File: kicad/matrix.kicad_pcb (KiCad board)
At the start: 2 copper layers, 20 parts, among them J1 Conn_01x08, Q1 2N7002DW-7-F, Q2 2N7002DW-7-F, Q3 2N7002DW-7-F, Q4 2N7002DW-7-F, Q5 2N7002DW-7-F, Q6 2N7002DW-7-F, Q7 2N7002DW-7-F, Q8 2N7002DW-7-F, U1 TLC59025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

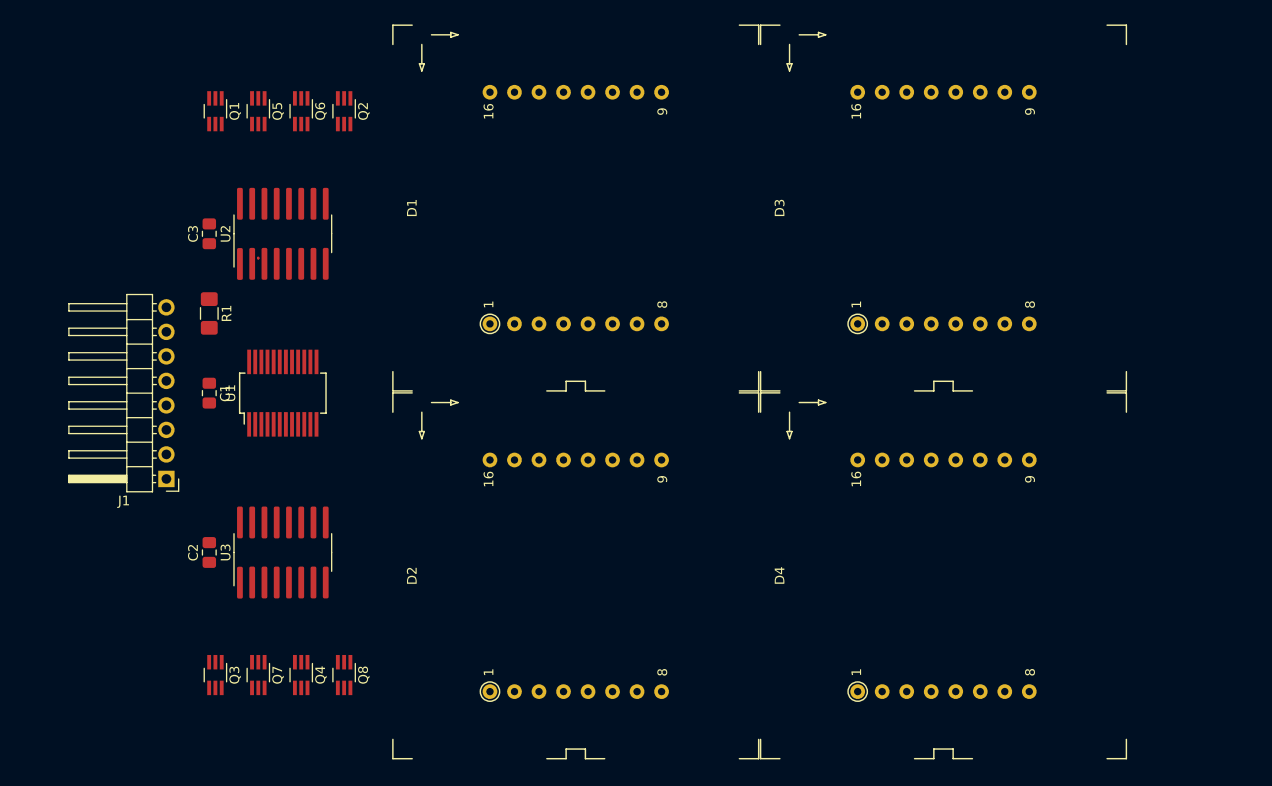
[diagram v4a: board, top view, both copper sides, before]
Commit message: OshPark design rules and copper GND pour
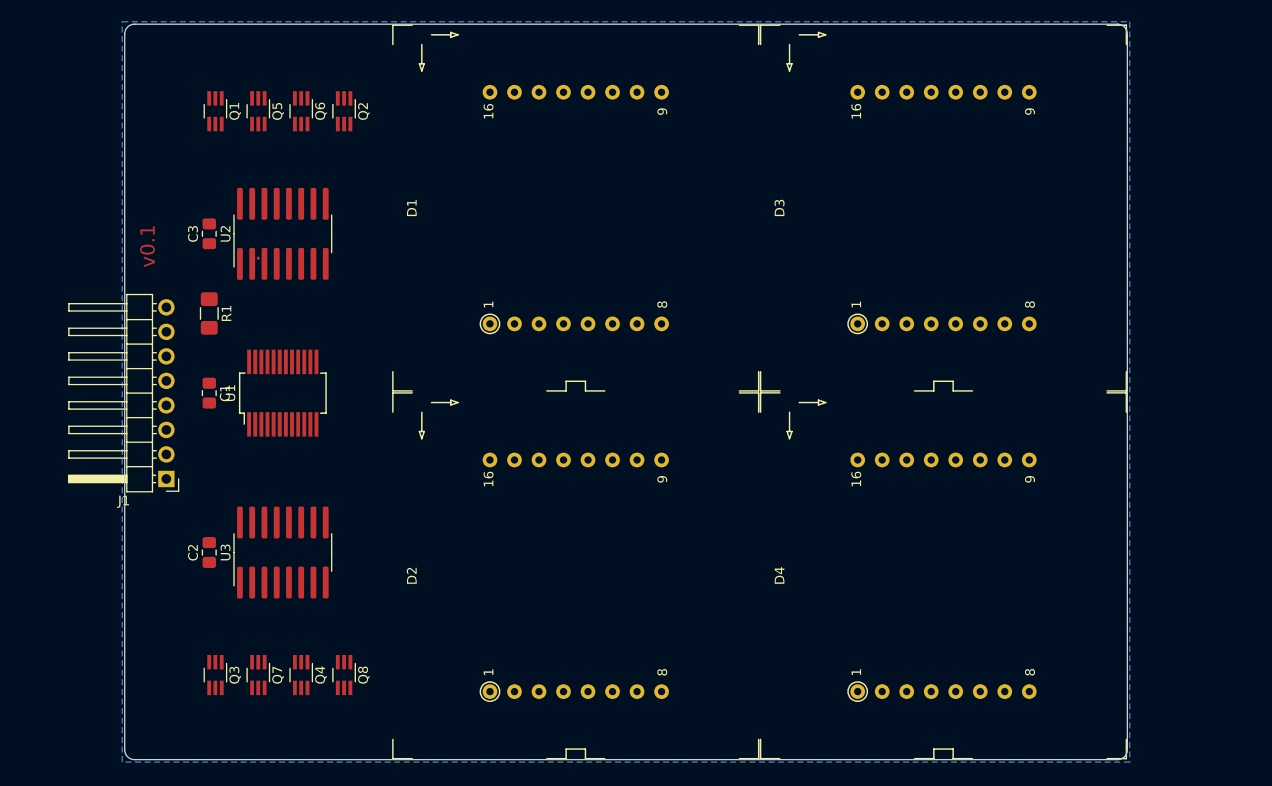
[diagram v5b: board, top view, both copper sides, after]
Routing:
- added copper zone on B.Cu, net GND
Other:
- board outline added: 103.9 x 76.2 mm
- net class Default: clearance 0.2 -> 0.1524; trace_width 0.25 -> 0.1524; via_dia 0.8 -> 0.508; via_drill 0.4 -> 0.254
- net class Power added: clearance 0.1524, trace_width 0.3048, via_dia 0.508, via_drill 0.254
- rule trace_clearance: 0.2 -> 0.1524
- rule trace_min: 0.2 -> 0.1524
- rule via_min_drill: 0.3 -> 0.254
- rule via_min_size: 0.4 -> 0.508
- board text added: "v0.1"
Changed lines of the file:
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@@
   (general
     (thickness 1.6)
-    (drawings 0)
+    (drawings 9)
     (tracks 2)
     (zones 0)
@@
     (0 F.Cu signal)
     (31 B.Cu signal)
-    (32 B.Adhes user)
-    (33 F.Adhes user)
-    (34 B.Paste user)
-    (35 F.Paste user)
     (36 B.SilkS user)
     (37 F.SilkS user)
     (38 B.Mask user)
     (39 F.Mask user)
-    (40 Dwgs.User user)
     (41 Cmts.User user)
-    (42 Eco1.User user)
-    (43 Eco2.User user)
     (44 Edge.Cuts user)
     (45 Margin user)
     (46 B.CrtYd user)
     (47 F.CrtYd user)
-    (48 B.Fab user)
-    (49 F.Fab user)
   )
   (setup
-    (last_trace_width 0.25)
-    (trace_clearance 0.2)
+    (last_trace_width 0.1524)
+    (user_trace_width 0.1524)
+    (user_trace_width 0.3048)
+    (trace_clearance 0.1524)
     (zone_clearance 0.508)
     (zone_45_only no)
-    (trace_min 0.2)
-    (via_size 0.8)
-    (via_drill 0.4)
-    (via_min_size 0.4)
-    (via_min_drill 0.3)
+    (trace_min 0.1524)
+    (via_size 0.508)
+    (via_drill 0.254)
+    (via_min_size 0.508)
+    (via_min_drill 0.254)
     (uvia_size 0.3)
     (uvia_drill 0.1)
@@
   (net 60 /ROWCLK)
   (net_class Default "This is the default net class."
-    (clearance 0.2)
-    (trace_width 0.25)
-    (via_dia 0.8)
-    (via_drill 0.4)
+    (clearance 0.1524)
+    (trace_width 0.1524)
+    (via_dia 0.508)
+    (via_drill 0.254)
     (uvia_dia 0.3)
     (uvia_drill 0.1)
@@
     (add_net "Net-(U3-Pad9)")
     (add_net VDD)
+  )
+  (net_class Power ""
+    (clearance 0.1524)
+    (trace_width 0.3048)
+    (via_dia 0.508)
+    (via_drill 0.254)
+    (uvia_dia 0.3)
+    (uvia_drill 0.1)
   )
   (module local:LED_8x8_3MM_38x38MM (layer F.Cu)
@@
     )
   )
+  (gr_text v0.1 (at 127.635 60.325 90) (layer F.Cu)
+    (effects (font (size 1.5 1.5) (thickness 0.3)))
+  )
+  (gr_arc (start 228.092 38.354) (end 229.108 38.354) (angle -90) (layer Edge.Cuts) (width 0.05))
+  (gr_arc (start 228.092 112.522) (end 228.092 113.538) (angle -90) (layer Edge.Cuts) (width 0.05))
+  (gr_arc (start 126.238 112.522) (end 125.222 112.522) (angle -90) (layer Edge.Cuts) (width 0.05))
+  (gr_arc (start 126.238 38.354) (end 126.238 37.338) (angle -90) (layer Edge.Cuts) (width 0.05))
+  (gr_line (start 126.238 37.338) (end 228.092 37.338) (layer Edge.Cuts) (width 0.05))
+  (gr_line (start 125.222 112.522) (end 125.222 38.354) (layer Edge.Cuts) (width 0.05))
+  (gr_line (start 228.092 113.538) (end 126.238 113.538) (layer Edge.Cuts) (width 0.05))
+  (gr_line (start 229.108 38.354) (end 229.108 112.522) (layer Edge.Cuts) (width 0.05))
   (segment (start 139.065 61.595) (end 139.05501 61.595) (width 0.25) (layer F.Cu) (net 0))
   (segment (start 139.05501 61.595) (end 139.05501 61.53) (width 0.25) (layer F.Cu) (net 0))
+  (zone (net 36) (net_name GND) (layer B.Cu) (hatch edge 0.508)
+    (connect_pads (clearance 0.508))
+    (min_thickness 0.254)
+    (fill yes (arc_segments 32) (thermal_gap 0.508) (thermal_bridge_width 0.508))
+    (polygon
+      (pts
+        (xy 229.362 113.792) (xy 124.968 113.792) (xy 124.968 37.084) (xy 229.362 37.084)
+      )
+    )
+  )
 )

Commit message: Wire up cathodes
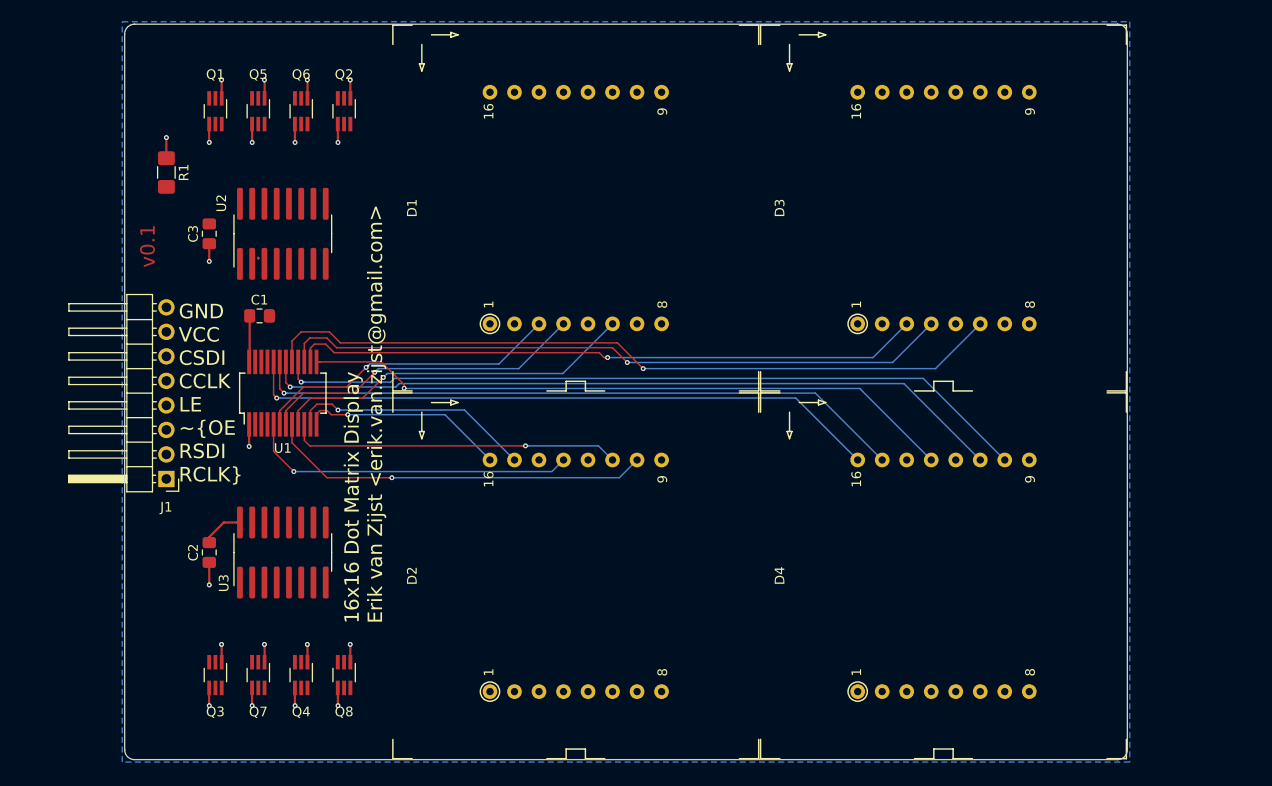
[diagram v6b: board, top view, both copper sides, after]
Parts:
- moved R1 15.3 mm to (129.5, 52.7)
- moved C1 9.55 mm to (139.2, 67.6), turned to 0 degrees
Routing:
- net /COL11: track 0.00 -> 78.8 mm, vias 0 -> 1
- net /COL13: track 0.00 -> 77.7 mm, vias 0 -> 1
- net /COL12: track 0.00 -> 77.4 mm, vias 0 -> 1
- net /COL10: track 0.00 -> 69.8 mm, vias 0 -> 1
- net /COL14: track 0.00 -> 68.3 mm, vias 0 -> 1
- net /COL8: track 0.00 -> 68.1 mm, vias 0 -> 1
- net /COL15: track 0.00 -> 66.7 mm, vias 0 -> 1
- net /COL9: track 0.00 -> 65.4 mm, vias 0 -> 1
- net /COL3: track 0.00 -> 39.9 mm, vias 0 -> 1
- net GND: track 0.00 -> 38.7 mm, vias 0 -> 20
- net /COL4: track 0.00 -> 37.7 mm, vias 0 -> 1
- net /COL5: track 0.00 -> 34.4 mm, vias 0 -> 1
- net /COL0: track 0.00 -> 34.2 mm, vias 0 -> 1
- net /COL2: track 0.00 -> 33.9 mm, vias 0 -> 1
- net /COL1: track 0.00 -> 32.0 mm, vias 0 -> 1
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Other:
- net class Default: trace_width 0.1524 -> 0.2286
- board text added: "16x16 Dot Matrix Display Erik van Zijst <erik.van.zijst@gmail.com>"
- board text added: "GND VCC CSDI CCLK LE ~OE RSDI RCLK"

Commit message: Switch to P-channel FETs in SOIC-8 package
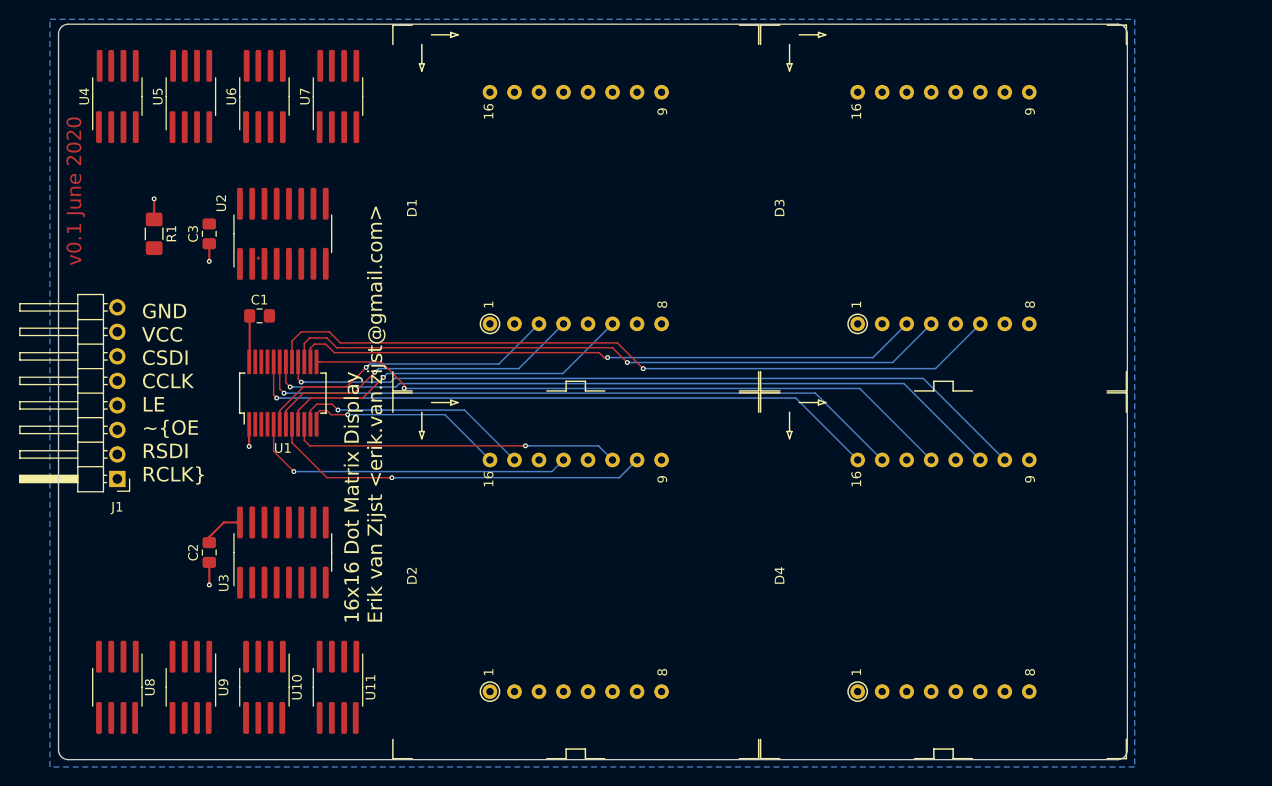
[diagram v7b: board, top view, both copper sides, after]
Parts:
- removed Q1, Q2, Q3, Q4, Q5, Q6, Q7, Q8: 2N7002DW-7-F, Package_TO_SOT_SMD:SOT-363_SC-70-6_Handsoldering
- added U10: P-FET, local:SOIC-8_3.9x4.9mm_P1.27mm_widepads, F.Cu at (139.7, 106.0)
- added U11: P-FET, local:SOIC-8_3.9x4.9mm_P1.27mm_widepads, F.Cu at (147.3, 106.0)
- added U4: P-FET, local:SOIC-8_3.9x4.9mm_P1.27mm_widepads, F.Cu at (124.5, 44.8)
- added U5: P-FET, local:SOIC-8_3.9x4.9mm_P1.27mm_widepads, F.Cu at (132.1, 44.8)
- added U6: P-FET, local:SOIC-8_3.9x4.9mm_P1.27mm_widepads, F.Cu at (139.7, 44.8)
- added U7: P-FET, local:SOIC-8_3.9x4.9mm_P1.27mm_widepads, F.Cu at (147.3, 44.8)
- added U8: P-FET, local:SOIC-8_3.9x4.9mm_P1.27mm_widepads, F.Cu at (124.5, 106.0)
- added U9: P-FET, local:SOIC-8_3.9x4.9mm_P1.27mm_widepads, F.Cu at (132.1, 106.0)
- moved R1 6.48 mm to (128.3, 59.1)
- moved J1 5.08 mm to (124.5, 84.5)
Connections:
- C3 pad 1: GND -> VDD
- C3 pad 2: VDD -> GND
- U1 pad 22: Net-(U1-Pad22) -> (no net)
- U3 pad 9: Net-(U3-Pad9) -> (no net)
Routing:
- net GND: track 38.7 -> 6.76 mm, vias 20 -> 3
- net VDD: track 9.16 -> 11.0 mm, vias 0 -> 1
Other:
- board size 103.9 x 76.2 mm -> 110.7 x 76.2 mm
- board text added: "v0.1 June 2020"
- board text removed: "v0.1"

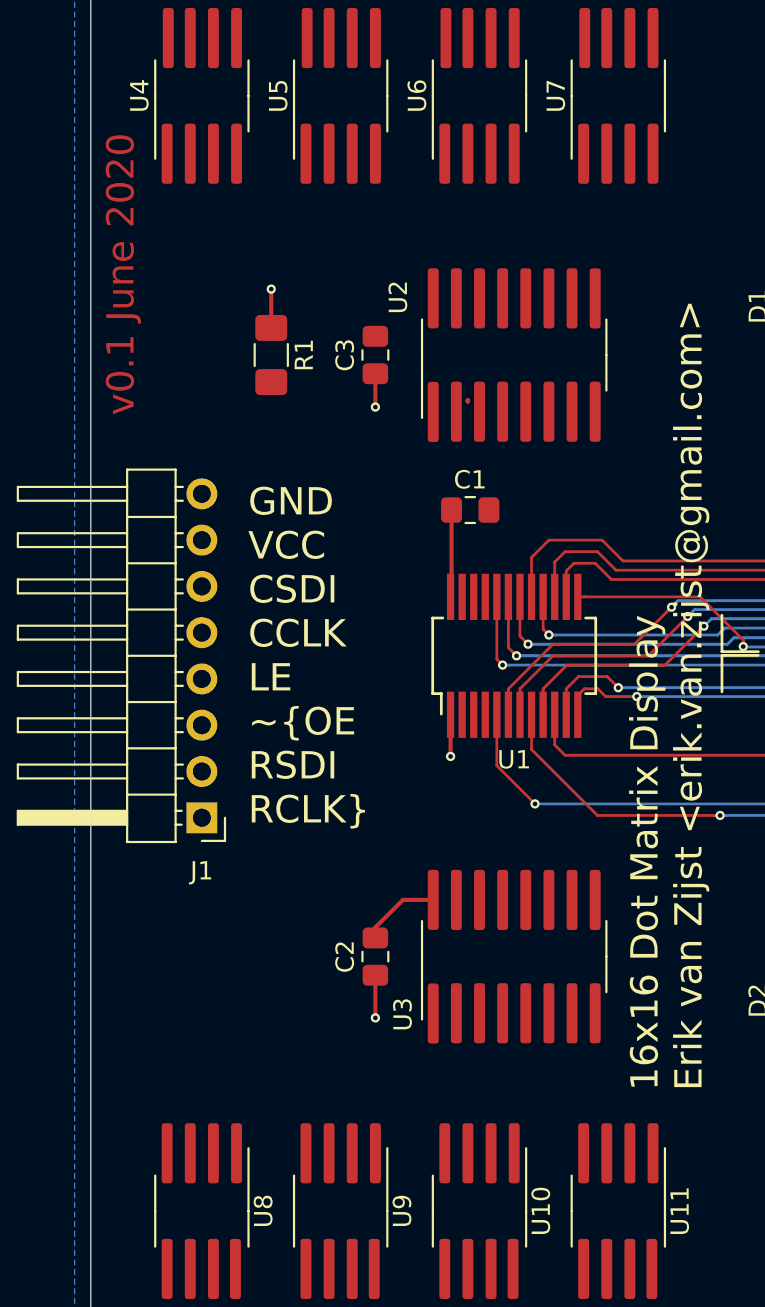
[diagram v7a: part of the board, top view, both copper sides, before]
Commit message: Add power net
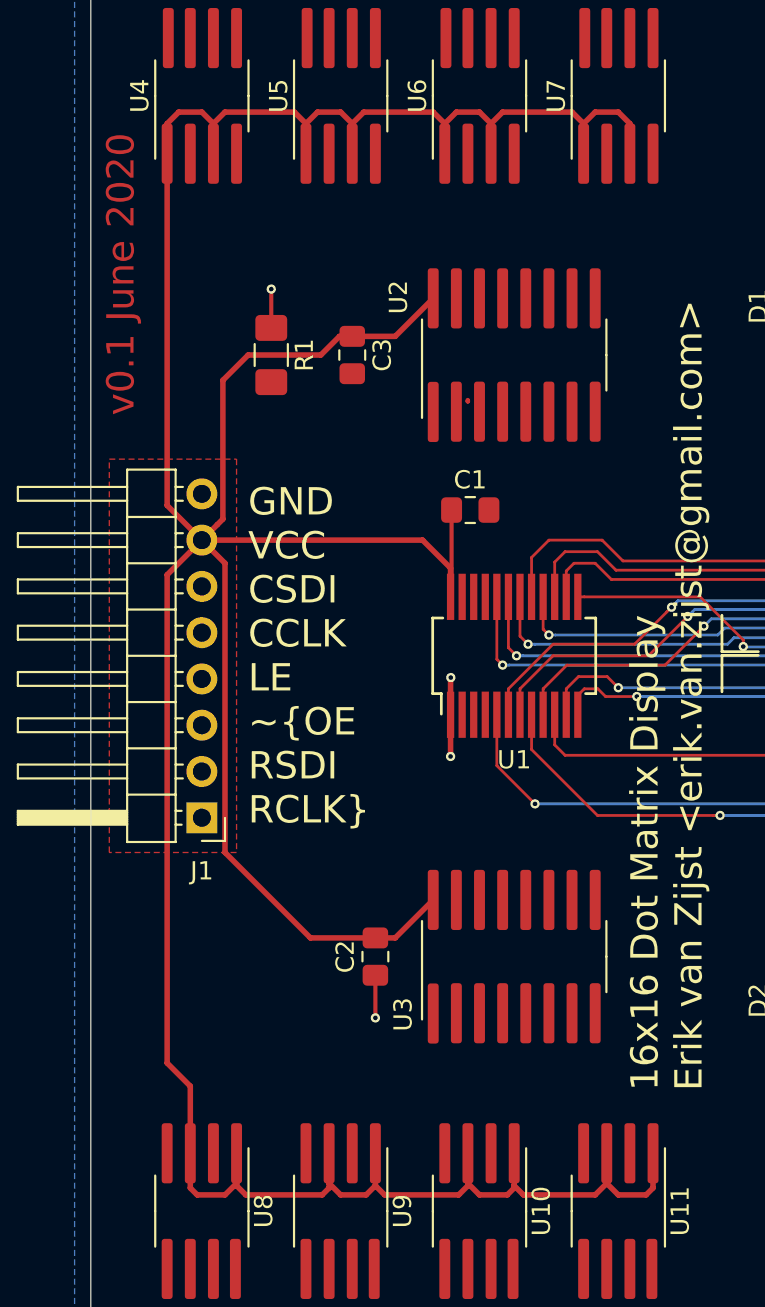
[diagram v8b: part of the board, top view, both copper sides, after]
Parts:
- moved C3 1.27 mm to (132.7, 59.1), turned to 270 degrees
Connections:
- U1 pad 22: (no net) -> Net-(U1-Pad22)
- U10 pad 1: Net-(U10-Pad1) -> VDD
- U10 pad 3: Net-(U10-Pad1) -> VDD
- U11 pad 1: Net-(U10-Pad1) -> VDD
- U11 pad 3: Net-(U10-Pad1) -> VDD
- U3 pad 9: (no net) -> Net-(U3-Pad9)
- U4 pad 1: Net-(U10-Pad1) -> VDD
- U4 pad 3: Net-(U10-Pad1) -> VDD
- U5 pad 1: Net-(U10-Pad1) -> VDD
- U5 pad 3: Net-(U10-Pad1) -> VDD
- U6 pad 1: Net-(U10-Pad1) -> VDD
- U6 pad 3: Net-(U10-Pad1) -> VDD
- U7 pad 1: Net-(U10-Pad1) -> VDD
- U7 pad 3: Net-(U10-Pad1) -> VDD
- U8 pad 1: Net-(U10-Pad1) -> VDD
- U8 pad 3: Net-(U10-Pad1) -> VDD
- U9 pad 1: Net-(U10-Pad1) -> VDD
- U9 pad 3: Net-(U10-Pad1) -> VDD
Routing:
- net VDD: track 11.0 -> 225.7 mm, vias 1 -> 0
- net GND: track 6.76 -> 8.81 mm, vias 3 -> 4
- added copper zone on F.Cu, net VDD
